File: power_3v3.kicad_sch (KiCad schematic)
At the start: 21 parts, among them U12 TPS7A2033PDBVR, U7 TPS62913RPUR, U8 USBLC6-2SC6

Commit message: Remove buzzer; passives to 0201/0402; GPIO28 to spare-IO block
Buzzer pads J15, driver Q20/D22/R33/R34 and the BUZZ nets removed; GPIO28
now terminates on J16 pin 12 (was a second GND). Resistors 0201, caps
<= 4.7 uF 0402, 22 uF/10 V 0603, 22 uF/25 V and 10 uF/50 V 0805, 47 uF
0805; USB net-class clearance 0.18 mm so the 0201 series resistors on the
pair pass DRC. Board regenerated at 50 x 50 mm (courtyard fill 63.5 %);
DRC unrouted-only. 134 components, 105 nets; ERC 0/0, 213 pin mappings,
run_power_checks PASS, audit 134/134.

Co-Authored-By: Claude Fable 5.1 <noreply@anthropic.com>
Claude-Session: https://claude.ai/code/session_01U6Ud7JA3CDTJZVcZZr5sx1
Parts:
- C10, C11, C12: value 22u / 10 V X7S, 1st-stage COUT -> 22u / 10 V X5R 0603 GRM188R61A226ME15, 1st-stage COUT (~40% DC-bias loss at 3.3 V); footprint Capacitor_SMD:C_0805_2012Metric -> Capacitor_SMD:C_0603_1608Metric
- C13: value 470n / 16 V X7R 0603, NR/SS soft-start + noise filter (5 ms) -> 470n / 16 V X7R 0402, NR/SS soft-start + noise filter (5 ms); footprint Capacitor_SMD:C_0603_1608Metric -> Capacitor_SMD:C_0402_1005Metric
- C23, C24: value 22u / 10 V X7S, 2nd-stage Cf (post-bead) -> 22u / 10 V X5R 0603 GRM188R61A226ME15, 2nd-stage Cf post-bead (~40% DC-bias loss at 3.3 V); footprint Capacitor_SMD:C_0805_2012Metric -> Capacitor_SMD:C_0603_1608Metric
- C25: value 1u / 10 V X7R 0603, LDO input -> 1u / 10 V X7R 0402, LDO input; footprint Capacitor_SMD:C_0603_1608Metric -> Capacitor_SMD:C_0402_1005Metric
- C26: value 1u / 10 V X7R 0603, LDO output, ESR <=100 mOhm -> 1u / 10 V X7R 0402, LDO output, ESR <=100 mOhm; footprint Capacitor_SMD:C_0603_1608Metric -> Capacitor_SMD:C_0402_1005Metric
- R10, R7, R8, R9: footprint Resistor_SMD:R_0402_1005Metric -> Resistor_SMD:R_0201_0603Metric
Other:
- note added: "PASSIVE PACKAGES (DESIGN_SPEC "Physical design"): resistors are 0201, ceramics <= 4.7 uF are 0402 and the 10-22 uF ceramics are 0603. C10/C11/C12 (1st-stage COUT) and C23/C24 (post-bead Cf) are 22 uF / 10 V X5R 0603 (GRM188R61A226ME15): at 3.3 V DC bias an X5R 22 uF 0603 keeps roughly 60 % of its nominal value, so the 66 uF nominal of the first stage is ~40 uF effective and the 44 uF post-bead st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"

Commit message: Flash socket becomes an optional back-side expansion; ESC row on the back edge; C19 100 uF
U24 (SOIC-8 150 mil) and its caps C62/C63 are DNP, excluded from the BOM
and placed flipped on the back with a legend ("FLASH / PSRAM EXPANSION,
SOIC-8 150mil, QMI CS1, W25Q64JVSSIQ or APS6404L-3SQR-SN"); the RP2354B's
internal 2 MB flash and the microSD cover firmware and logging. The ESC pad
row J3 sits along the left edge on the back, like the DBG row on the bottom
edge. C19 (V5_SYS bulk) reduced from 220 uF D-case to 100 uF 6.3 V B-case:
the ngspice decks now use CPOLY=100u and every handover predicate still
passes (worst-case V5_SYS min 4.37 V). Board 46.6 x 41.2 mm; DRC
unrouted-only; ERC 0/0, checker PASS, audit 140/140.

Co-Authored-By: Claude Fable 5.1 <noreply@anthropic.com>
Claude-Session: https://claude.ai/code/session_01U6Ud7JA3CDTJZVcZZr5sx1
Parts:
- C19: value 220u / 10 V polymer, ESR ~40 mOhm -> 100u / 6.3 V polymer, ESR <= 40 mOhm (e.g. Panasonic 6TPE100MAZB or KEMET T520/T530 B case); footprint Capacitor_Tantalum_SMD:CP_EIA-7343-31_Kemet-D -> Capacitor_Tantalum_SMD:CP_EIA-3528-21_Kemet-B

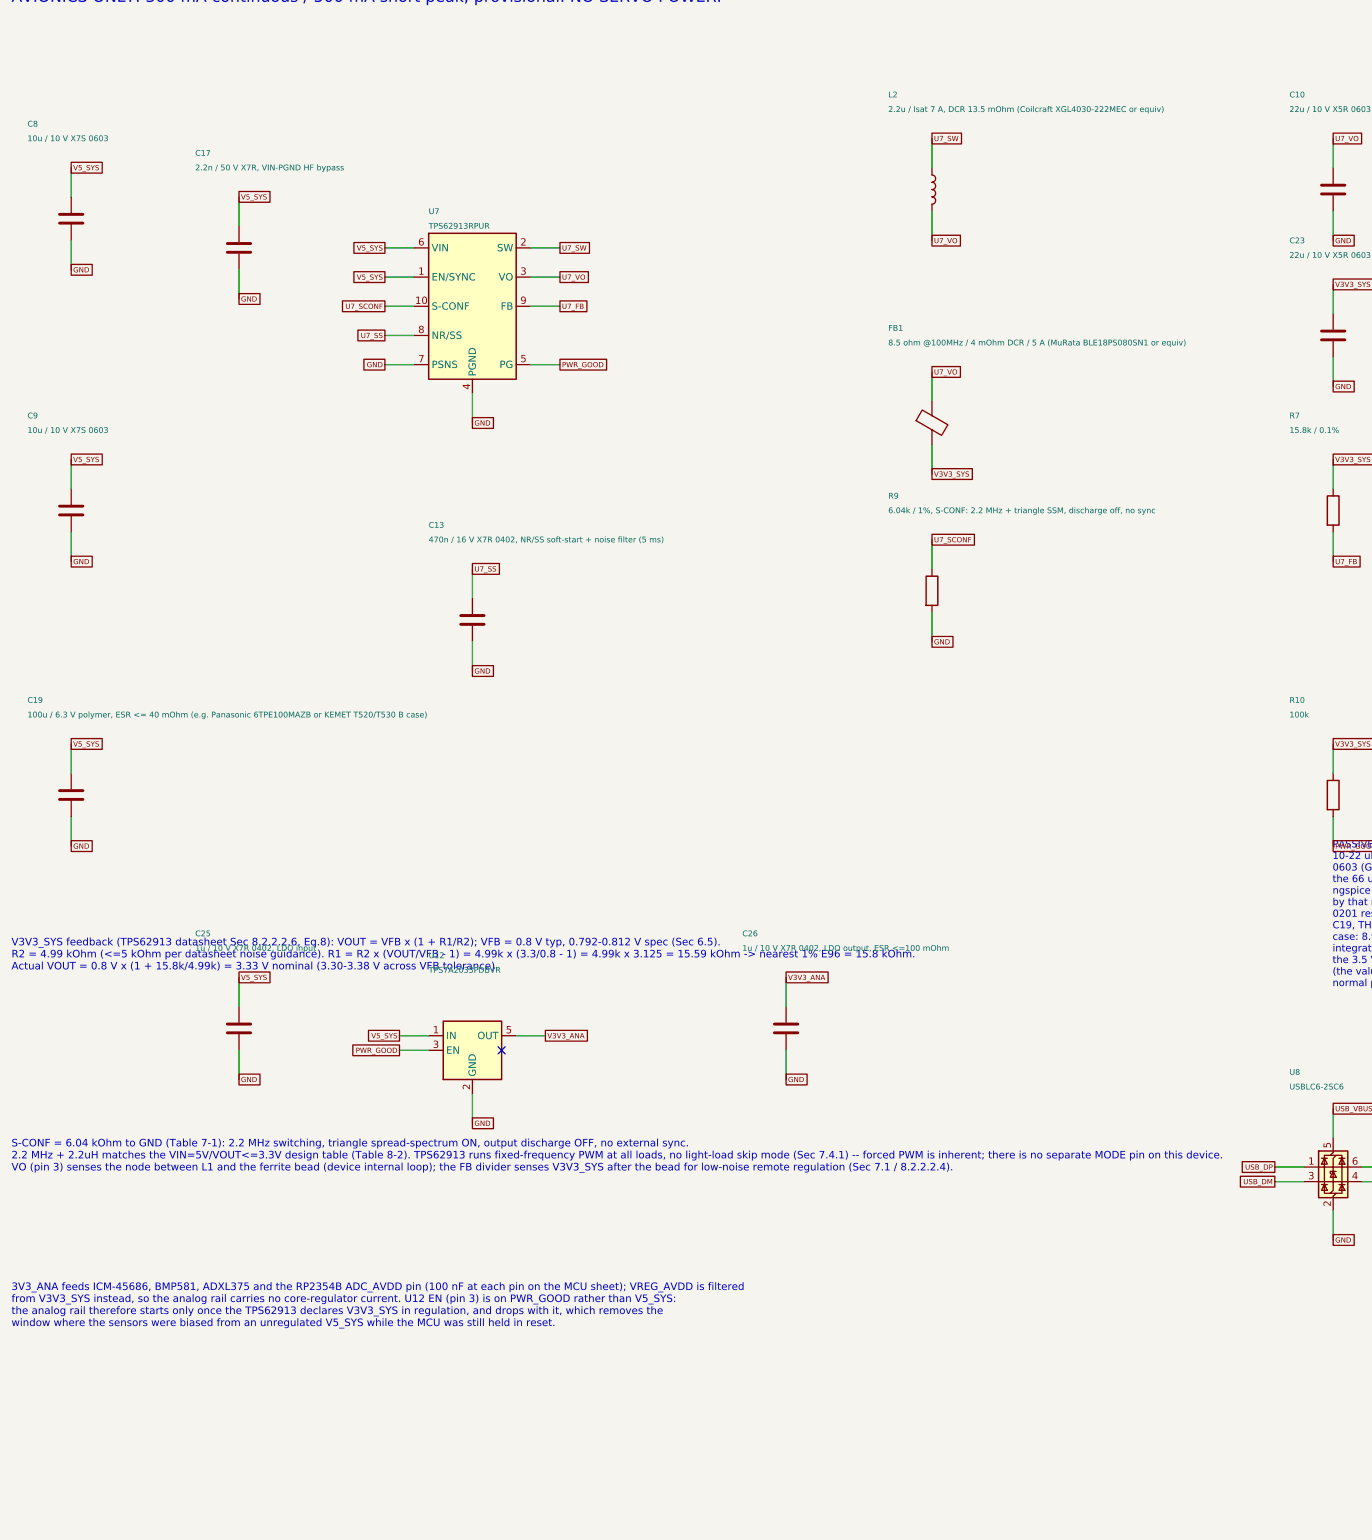
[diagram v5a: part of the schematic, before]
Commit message: Flash-socket caps back on the front, minimal socket silk; L2 to XGL3020-222
C62/C63 (U24 decoupling) are fitted on the front again, so a user adding a
flash or PSRAM chip to the back-side SOIC-8 socket only solders the chip;
the back legend is reduced to "FLASH" / "SOIC-8" plus the pin-1 mark, and
the compatible parts (150-mil SOIC-8 QSPI NOR: W25Q16/32/64JVSS, GD25Q32C/
64C, MX25L3233F/6433F; QSPI PSRAM: APS6404L-3SQR-SN, ESP-PSRAM64H, IPS6404L,
LY68L6400) are documented in DESIGN_SPEC/LIBRARIES.

L2 (TPS62913 3.3 V buck inductor) shrinks from XGL4030-222 (4x4x3.1) to
Coilcraft XGL3020-222MEC (3x3x2.0; Isat 2.2 A @20 %, 2.85 A @30 %, DCR
30.5 mOhm, Doc 1776 Rev 02/19/26) against a ~0.95 A peak; project footprint
from the Coilcraft land pattern, vendor STEP aligned and verified against
copper. L3 stays XGL4030-472: its floor is the AP63205's 3.1 A current-limit
ceiling and the XGL4020 shares the 4x4 land pattern. Board 46.6 x 41.2 mm;
DRC unrouted-only; ERC 0/0, checker PASS, ngspice PASS, audit 140/140.

Co-Authored-By: Claude Fable 5.1 <noreply@anthropic.com>
Claude-Session: https://claude.ai/code/session_01U6Ud7JA3CDTJZVcZZr5sx1
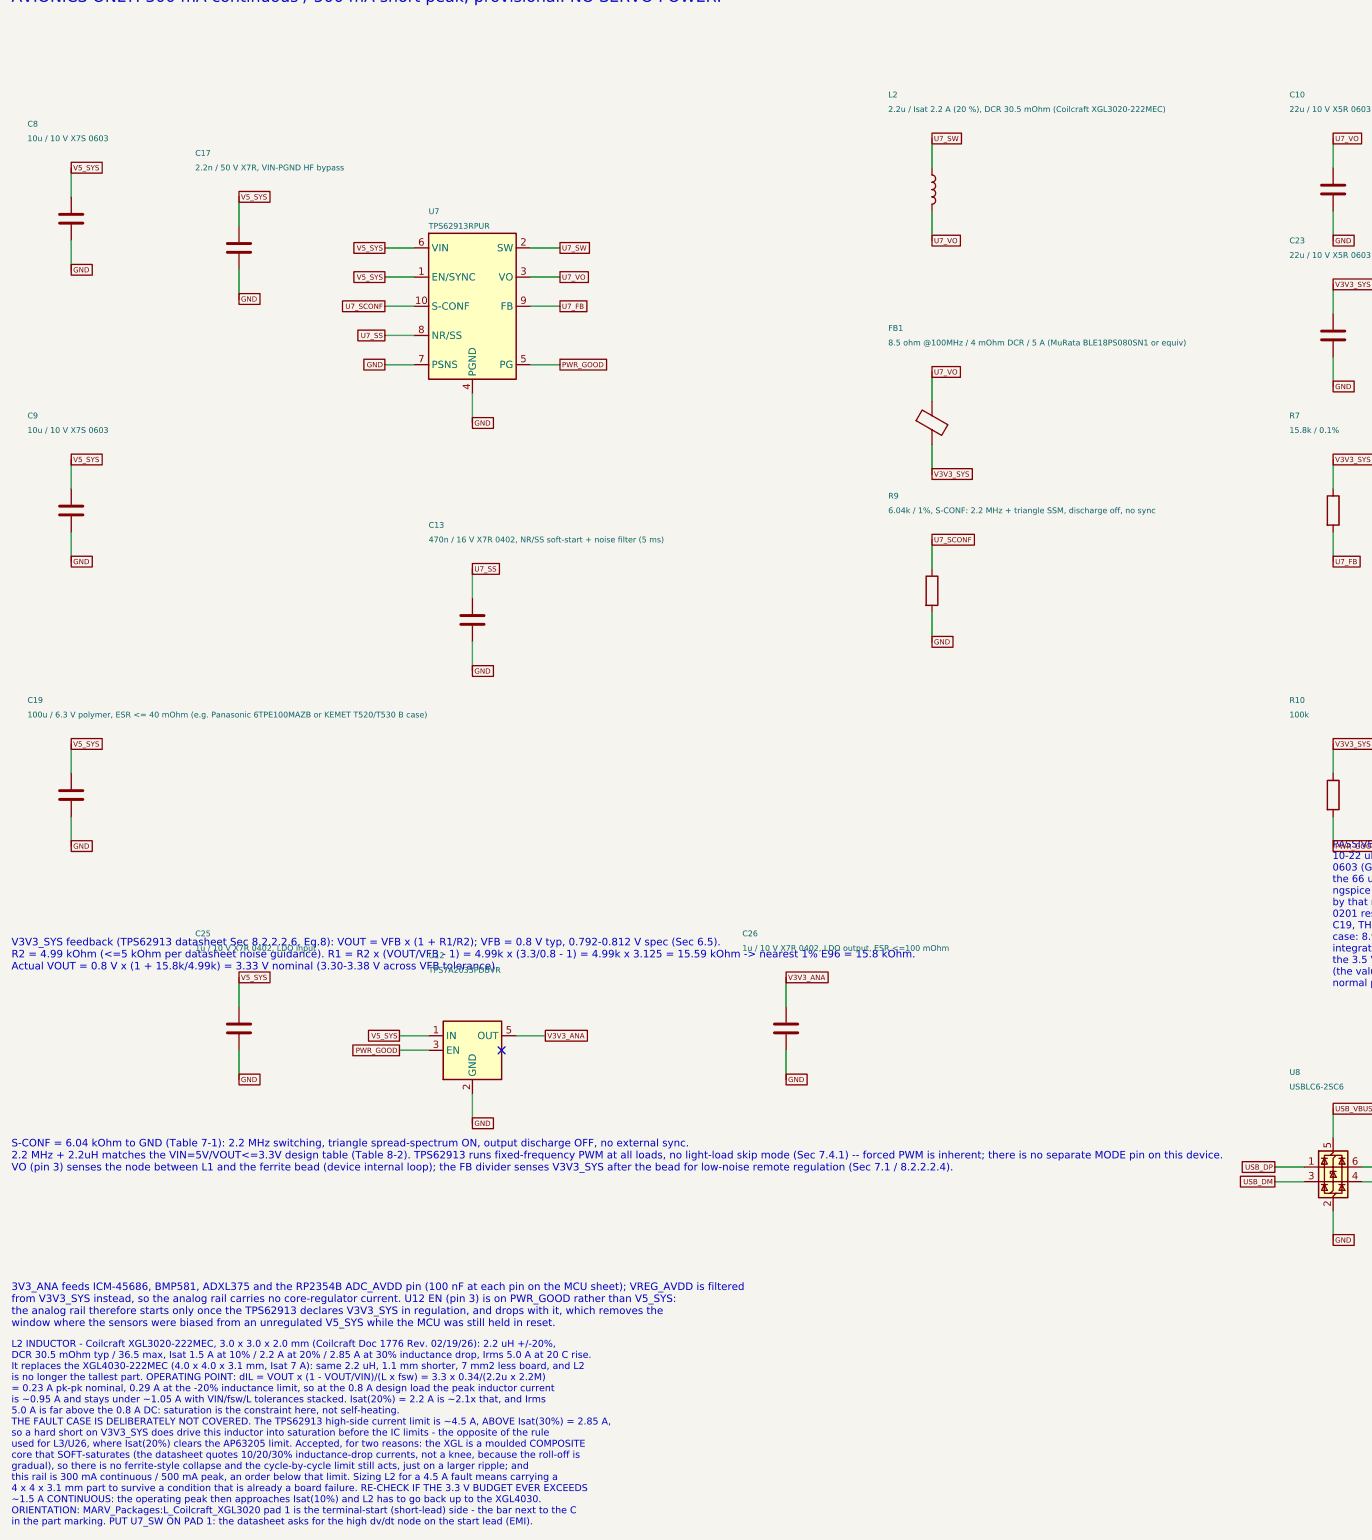
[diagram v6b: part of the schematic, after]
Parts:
- L2: value 2.2u / Isat 7 A, DCR 13.5 mOhm (Coilcraft XGL4030-222MEC or equiv) -> 2.2u / Isat 2.2 A (20 %), DCR 30.5 mOhm (Coilcraft XGL3020-222MEC); footprint MARV_Packages:L_Coilcraft_XxL4030 -> MARV_Packages:L_Coilcraft_XGL3020
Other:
- note added: "L2 INDUCTOR - Coilcraft XGL3020-222MEC, 3.0 x 3.0 x 2.0 mm (Coilcraft Doc 1776 Rev. 02/19/26): 2.2 uH +/-20%, DCR 30.5 mOhm typ / 36.5 max, Isat 1.5 A at 10% / 2.2 A at 20% / 2.85 A at 30% inductance drop, Irms 5.0 A at 20 C rise. It replaces the XGL4030-222MEC (4.0 x 4.0 x 3.1 mm, Isat 7 A): same 2.2 uH, 1.1 mm shorter, 7 mm2 less board, and L2 is no longer the tallest part. OPERATING POINT: dIL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"

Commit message: JLCPCB sourcing: Basic-part refactor, LCSC numbers in the schematic, order files and audit
Parts audited line by line against JLCPCB's live catalogue (tools/jlc/,
reports/jlc-audit.md). Resistors move 0201 -> 0402 (JLC's Basic library has
no 0201 resistor), the U7 FB divider becomes 10k/3.16k 0.1 % (15.8k 0.1 % is
not stocked), Y1 becomes TAXM12M4RFBCCT2T (CL 12 pF) with 18 pF loads, L2/L3
become CJIANG FTC303020D2R2MBCA / FTC404030S4R7MGCA (stocked; Isat 5.5 A /
6.0 A at 30 %, footprints + models vendored from KiCad), the 22 uF/25 V and
10 uF lines move to Basic parts. The U24 default fit is W25Q32JVSNIQ (the
W25Q64JVSSIQ is a 208-mil part and never fitted the 150-mil socket).

Every fitted symbol carries a hidden LCSC property stamped from
tools/jlc/lcsc_map.csv; tools/jlc/export_jlc.py writes reports/jlc-bom.csv
and reports/jlc-cpl.csv (top-side SMT, headers unpopulated, U24 DNP).
Result: 46 unique parts, 16 Basic / 1 Preferred / 29 Extended (was 9/1/35),
extended-fee estimate $87 (was $105), $45.68 per board at 10 (was $52.97 with
L2 unsourced). DESIGN_SPEC gains a Manufacturing (JLCPCB) section with the
quote parameters. Board rebuilt (0 fit/geometry, DRC unrouted-only); ERC
0/0, checker PASS, ngspice PASS, audit 140/140.

Co-Authored-By: Claude Fable 5.1 <noreply@anthropic.com>
Claude-Session: https://claude.ai/code/session_01U6Ud7JA3CDTJZVcZZr5sx1
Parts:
- C10, C11, C12, C23, C24: LCSC (none) -> C86295
- C13: LCSC (none) -> C471404
- C17: LCSC (none) -> C1531
- C19: LCSC (none) -> C79109
- C25, C26: LCSC (none) -> C52923
- C8, C9: LCSC (none) -> C96446
- FB1: LCSC (none) -> C3764407
- L2: value 2.2u / Isat 2.2 A (20 %), DCR 30.5 mOhm (Coilcraft XGL3020-222MEC) -> 2.2u / Isat 5.5 A (30 %), DCR 45 mOhm max (CJIANG FTC303020D2R2MBCA); footprint MARV_Packages:L_Coilcraft_XGL3020 -> MARV_Packages:L_Changjiang_FTC303020D; LCSC (none) -> C7423318
- R10: footprint Resistor_SMD:R_0201_0603Metric -> Resistor_SMD:R_0402_1005Metric; LCSC (none) -> C25741
- R7: value 15.8k / 0.1% -> 10k / 0.1%; footprint Resistor_SMD:R_0201_0603Metric -> Resistor_SMD:R_0402_1005Metric; LCSC (none) -> C190095
- R8: value 4.99k / 0.1% -> 3.16k / 0.1%; footprint Resistor_SMD:R_0201_0603Metric -> Resistor_SMD:R_0402_1005Metric; LCSC (none) -> C852759
- R9: footprint Resistor_SMD:R_0201_0603Metric -> Resistor_SMD:R_0402_1005Metric; LCSC (none) -> C25913
- U12: LCSC (none) -> C2862740
- U7: LCSC (none) -> C5189914
- U8: LCSC (none) -> C2687116
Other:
- note added: "L2 INDUCTOR - CJIANG FTC303020D2R2MBCA, 3.0 x 3.0 x 2.0 mm molded metal-composite (SZ CJIANG FTC series datasheet Rev 7.0 2025/11/05, the sheet LCSC serves for C7423318): 2.2 uH +/-20% at 1 MHz / 1.0 Vrms, DCR 37 mOhm typ / 45 max, Irms 4.7 A typ / 4.3 A worst case, Isat 6.0 A typ / 5.5 A worst case. THE CRITERIA ARE THE DATASHEET'S OWN NOTES 3 AND 4: Irms is the DC current for an approximate 40 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"
- note added: "PASSIVE PACKAGES (DESIGN_SPEC "Physical design"): resistors are 0402, ceramics <= 4.7 uF are 0402 and the 10-22 uF ceramics are 0603. RESISTORS ARE 0402, NOT 0201: JLCPCB has no Basic 0201 resistor of any value, so every 0201 line carried a per-unique-part Extended setup fee, and the 0.1 % values the U7 divider needs are not stocked in 0201 at all - see reports/jlc-audit.md. 0402 makes 8 of the 1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"
- note added: "V3V3_SYS feedback (TPS62913 datasheet Sec 8.2.2.2.6, Eq.8): VOUT = VFB x (1 + R1/R2); VFB = 0.8 V typ, 0.792-0.812 V spec (Sec 6.5). R2 = 3.16 kOhm (<=5 kOhm per datasheet noise guidance). R1 = R2 x (VOUT/VFB - 1) = 3.16k x 3.1625 = 9.99 kOhm -> E96 10.0 kOhm. Actual VOUT = 0.8 V x (1 + 10k/3.16k) = 0.8 x 4.16456 = 3.3316 V nominal, +0.05% off the 3.33 V the decks model. THE PAIR IS 10k / 3.16k, 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"
- note removed: "L2 INDUCTOR - Coilcraft XGL3020-222MEC, 3.0 x 3.0 x 2.0 mm (Coilcraft Doc 1776 Rev. 02/19/26): 2.2 uH +/-20%, DCR 30.5 mOhm typ / 36.5 max, Isat 1.5 A at 10% / 2.2 A at 20% / 2.85 A at 30% inductance drop, Irms 5.0 A at 20 C rise. It replaces the XGL4030-222MEC (4.0 x 4.0 x 3.1 mm, Isat 7 A): same 2.2 uH, 1.1 mm shorter, 7 mm2 less board, and L2 is no longer the tallest part. OPERATING POINT: dIL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"
- note removed: "PASSIVE PACKAGES (DESIGN_SPEC "Physical design"): resistors are 0201, ceramics <= 4.7 uF are 0402 and the 10-22 uF ceramics are 0603. C10/C11/C12 (1st-stage COUT) and C23/C24 (post-bead Cf) are 22 uF / 10 V X5R 0603 (GRM188R61A226ME15): at 3.3 V DC bias an X5R 22 uF 0603 keeps roughly 60 % of its nominal value, so the 66 uF nominal of the first stage is ~40 uF effective and the 44 uF post-bead st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"
- note removed: "V3V3_SYS feedback (TPS62913 datasheet Sec 8.2.2.2.6, Eq.8): VOUT = VFB x (1 + R1/R2); VFB = 0.8 V typ, 0.792-0.812 V spec (Sec 6.5). R2 = 4.99 kOhm (<=5 kOhm per datasheet noise guidance). R1 = R2 x (VOUT/VFB - 1) = 4.99k x (3.3/0.8 - 1) = 4.99k x 3.125 = 15.59 kOhm -> nearest 1% E96 = 15.8 kOhm. Actual VOUT = 0.8 V x (1 + 15.8k/4.99k) = 3.33 V nominal (3.30-3.38 V across VFB tolerance)."

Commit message: Schematic re-organised into 11 per-subsystem pages, drawn as wired blocks
Each subsystem now has its own sheet (RP2354B, USB/debug, ICM-45686, BMP581,
ADXL375, microSD, QSPI expansion, VBAT buck + ESC row, priority mux, 3.3 V
rail, IO block) with the IC's own decoupling, pull-ups, test points and
connectors placed beside it and wired, labels only for nets leaving the
block. Root sheet is an index. tools/build_power.py grows a small layout
engine (wire routing, junctions, decoupling ladders, note flow) with
self-checks for dangling wires and multi-net wire islands; the long design
notes are preserved verbatim as module constants.

Purely presentational: netlist fingerprint (tools/netlist_fingerprint.py,
new) is identical before and after, ERC 0, power checks pass. PCB footprint
paths re-pointed at the new sheet UUIDs by tools/relink_pcb_paths.py (new);
the board diff is path lines only, DRC unconnected count unchanged.
README/DESIGN_SPEC sheet lists updated; pre-change sheets and generator in
backups/pre-sheet-reorg-2026-09-16/.

Also carries the uncommitted work that preceded it: PCB routing, plane
stitching and route-analysis tools (tools/route_*.py, stitch_planes.py),
GPIO remap in PINOUT.md / check_power_netlist.py / setup_pcb.py, and the
grommet mounting-hole footprint update.

Co-Authored-By: Claude Fable 5.1 <noreply@anthropic.com>
Claude-Session: https://claude.ai/code/session_01Y51PayhRcgfdi3hVsfn4qg
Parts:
- removed U8: USBLC6-2SC6, Package_TO_SOT_SMD:SOT-23-6, symbol Power_Protection:USBLC6-2SC6
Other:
- note added: "1st-stage COUT (U7_VO)"
- note added: "2nd-stage Cf (post-bead, V3V3_SYS)"
- note added: "3.3 V system buck"
- note added: "Analog LDO -> V3V3_ANA"
- note added: "Feedback divider"
- note added: "POWER 3 - U7 TPS62913 BUCK (V5_SYS -> V3V3_SYS) AND U12 TPS7A20 LDO (-> V3V3_ANA) AVIONICS ONLY: 300 mA continuous / 500 mA short peak, provisional. NO SERVO POWER."
- note added: "V5_SYS input bulk"
- note added: "the usable rated current is the LESSER of the two, so this part is Irms-limited at 4.3 A, not saturation-limited. It replaces the Coilcraft XGL3020-222MEC, which is NOT ORDERABLE AT JLCPCB in any value (reports/jlc-audit.md section 6). Same 3.0 x 3.0 x 2.0 envelope, same shielded (closed magnetic circuit) construction, DCR 30.5 typ / 36.5 max -> 37 typ / 45 max mOhm, which costs ~4 mW at the 0.8 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"
- note removed: "AVIONICS ONLY: 300 mA continuous / 500 mA short peak, provisional. NO SERVO POWER."
- title: POWER 2 / 3.3 V system buck and analog LDO -> POWER 3 / 3.3 V system buck and analog LDO
- moved on the sheet: C10, C11, C12, C13, C17, C19, C23, C24, C25, C26, C8, C9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
